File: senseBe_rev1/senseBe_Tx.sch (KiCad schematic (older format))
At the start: 18 parts, among them Q5 SI2302, Q6 SI2302, Q7 SI2302, U3 AP3403

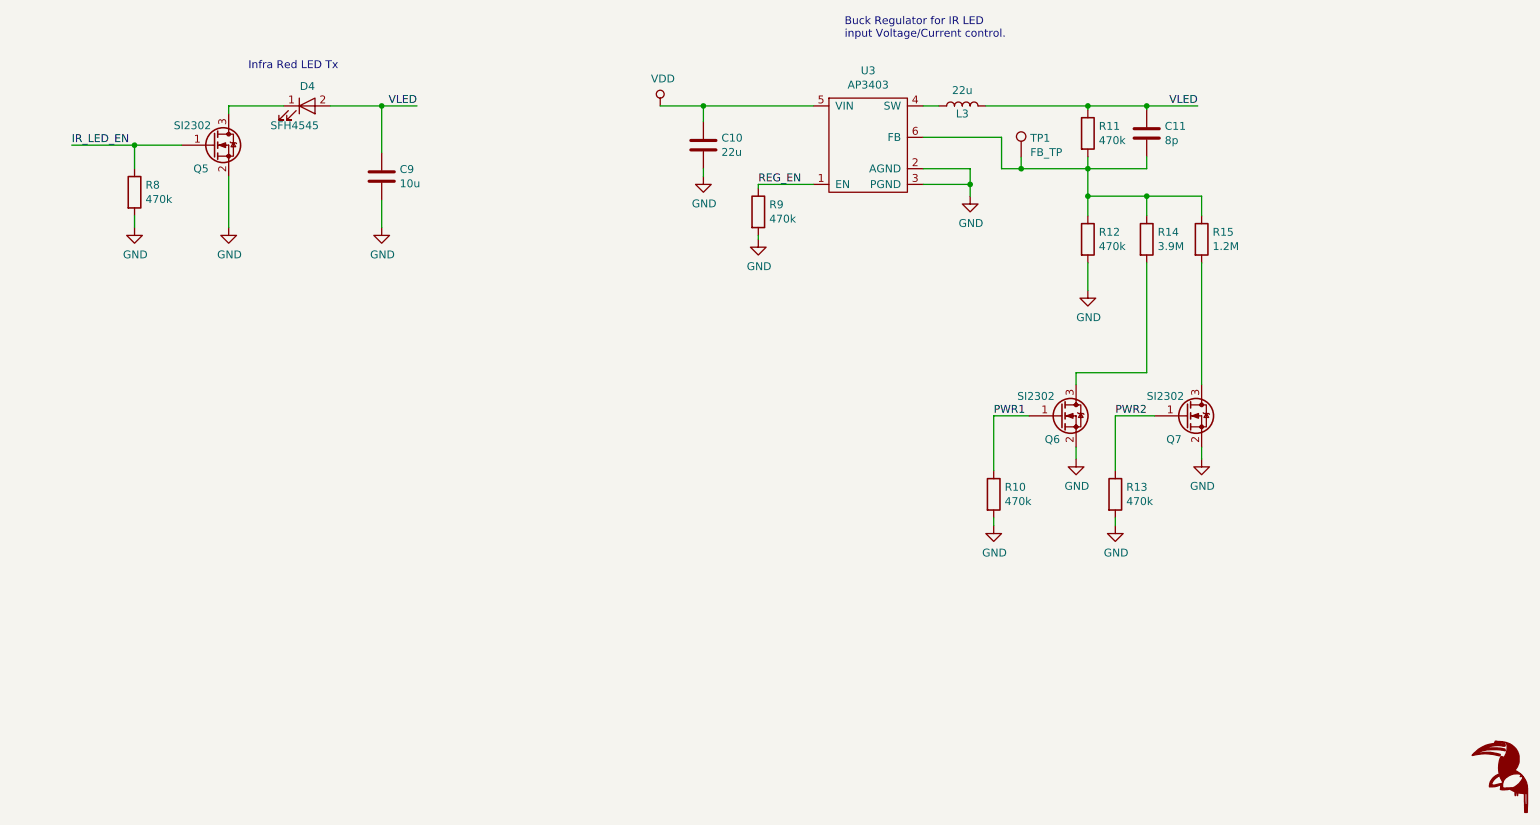
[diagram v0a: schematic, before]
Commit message: Completes Schematic and PCB Design.
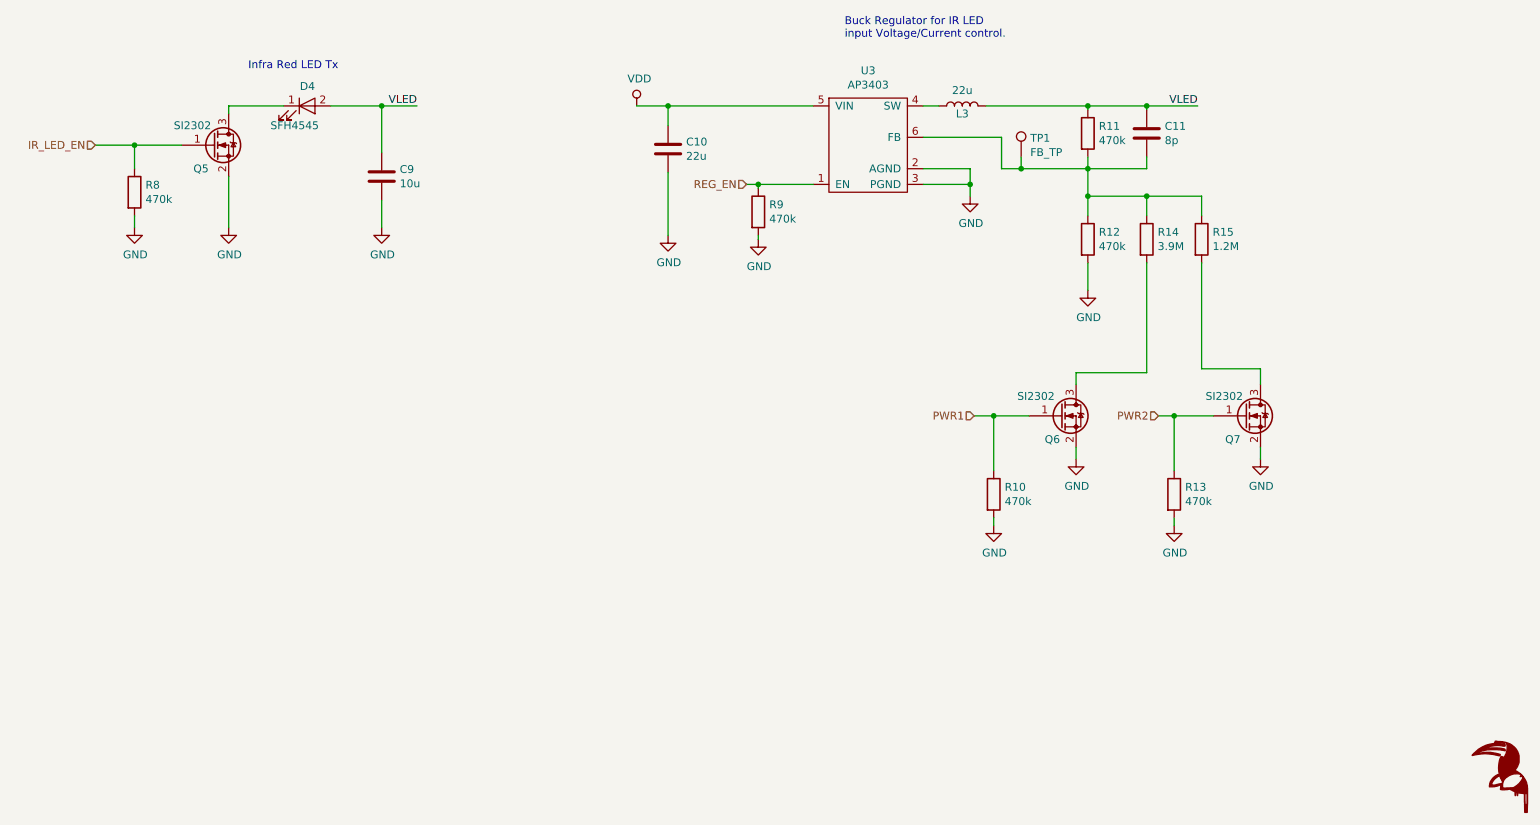
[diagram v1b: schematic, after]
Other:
- moved on the sheet: C10, Q7, R13
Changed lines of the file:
@@
 L senseBe_rev1-rescue:C-AP3403_LED_test-Ap3403_LED_test-rescue-senseBeTx_rev3-rescue-senseBe_rev1-rescue C?
 U 1 1 5C8021B2
-P 5775 2825
+P 5550 2850
 AR Path="/5C8021B2" Ref="C?"  Part="1"
 AR Path="/5C63BFE8/5C8021B2" Ref="C10"  Part="1"
-F 0 "C10" H 5890 2871 50  0000 L CNN
-F 1 "22u" H 5890 2780 50  0000 L CNN
-F 2 "senseBe_rev1_fp:C_0805_HandSoldering" H 5813 2675 50  0001 C CNN
-F 3 "~" H 5775 2825 50  0001 C CNN
-	1    5775 2825
+F 0 "C10" H 5665 2896 50  0000 L CNN
+F 1 "22u" H 5665 2805 50  0000 L CNN
+F 2 "senseBe_rev1_fp:C_0805_HandSoldering" H 5588 2700 50  0001 C CNN
+F 3 "~" H 5550 2850 50  0001 C CNN
+	1    5550 2850
 	1    0    0    -1
 $EndComp
@@
 L senseBe_rev1-rescue:GND-AP3403_LED_test-Ap3403_LED_test-rescue-senseBeTx_rev3-rescue-senseBe_rev1-rescue #PWR?
 U 1 1 5C8021CD
-P 5775 3025
+P 5550 3400
 AR Path="/5C8021CD" Ref="#PWR?"  Part="1"
 AR Path="/5C63BFE8/5C8021CD" Ref="#PWR0102"  Part="1"
-F 0 "#PWR0102" H 5775 2775 50  0001 C CNN
-F 1 "GND" H 5780 2852 50  0000 C CNN
-F 2 "" H 5775 3025 50  0001 C CNN
-F 3 "" H 5775 3025 50  0001 C CNN
-	1    5775 3025
-	1    0    0    -1
-$EndComp
-Wire Wire Line
-	5775 2975 5775 3025
-Wire Wire Line
-	5500 2575 5775 2575
-Wire Wire Line
-	5775 2575 5775 2675
-Text Label 6125 3075 0    50   ~ 0
-REG_EN
+F 0 "#PWR0102" H 5550 3150 50  0001 C CNN
+F 1 "GND" H 5555 3227 50  0000 C CNN
+F 2 "" H 5550 3400 50  0001 C CNN
+F 3 "" H 5550 3400 50  0001 C CNN
+	1    5550 3400
+	1    0    0    -1
+$EndComp
+Wire Wire Line
+	5550 3000 5550 3400
+Wire Wire Line
+	5350 2575 5550 2575
+Wire Wire Line
+	5550 2575 5550 2700
 Wire Wire Line
 	7175 2975 7475 2975
@@
 L senseBe_rev1-rescue:Q_NMOS_GSD-AP3403_LED_test-Ap3403_LED_test-rescue-senseBeTx_rev3-rescue-senseBe_rev1-rescue Q?
 U 1 1 5C80221D
-P 8850 4550
+P 9225 4550
 AR Path="/5C80221D" Ref="Q?"  Part="1"
 AR Path="/5C63BFE8/5C80221D" Ref="Q7"  Part="1"
-F 0 "Q7" H 8725 4400 50  0000 L CNN
-F 1 "SI2302" H 8600 4675 50  0000 L CNN
-F 2 "senseBeTx_rev3_fp:SOT-23_Handsoldering" H 9050 4650 50  0001 C CNN
-F 3 "~" H 8850 4550 50  0001 C CNN
-	1    8850 4550
+F 0 "Q7" H 9100 4400 50  0000 L CNN
+F 1 "SI2302" H 8975 4675 50  0000 L CNN
+F 2 "senseBeTx_rev3_fp:SOT-23_Handsoldering" H 9425 4650 50  0001 C CNN
+F 3 "~" H 9225 4550 50  0001 C CNN
+	1    9225 4550
 	1    0    0    -1
 $EndComp
@@
 L senseBe_rev1-rescue:GND-AP3403_LED_test-Ap3403_LED_test-rescue-senseBeTx_rev3-rescue-senseBe_rev1-rescue #PWR?
 U 1 1 5C80222B
-P 8950 4825
+P 9325 4825
 AR Path="/5C80222B" Ref="#PWR?"  Part="1"
 AR Path="/5C63BFE8/5C80222B" Ref="#PWR0106"  Part="1"
-F 0 "#PWR0106" H 8950 4575 50  0001 C CNN
-F 1 "GND" H 8955 4652 50  0000 C CNN
-F 2 "" H 8950 4825 50  0001 C CNN
-F 3 "" H 8950 4825 50  0001 C CNN
-	1    8950 4825
-	1    0    0    -1
-$EndComp
-Wire Wire Line
-	8950 4750 8950 4825
+F 0 "#PWR0106" H 9325 4575 50  0001 C CNN
+F 1 "GND" H 9330 4652 50  0000 C CNN
+F 2 "" H 9325 4825 50  0001 C CNN
+F 3 "" H 9325 4825 50  0001 C CNN
+	1    9325 4825
+	1    0    0    -1
+$EndComp
+Wire Wire Line
+	9325 4750 9325 4825
 Wire Wire Line
 	8150 4275 8150 4350
-Text Label 7625 4550 0    50   ~ 0
-PWR1
-Text Label 8400 4550 0    50   ~ 0
-PWR2
 $Comp
 L senseBe_rev1-rescue:Q_NMOS_GSD-AP3403_LED_test-Ap3403_LED_test-rescue-senseBeTx_rev3-rescue-senseBe_rev1-rescue Q?
@@
 Wire Wire Line
 	2750 3025 2750 3350
-Text Label 1750 2825 0    50   ~ 0
-IR_LED_EN
 Wire Wire Line
 	3725 3175 3725 3350
@@
 $EndComp
 Wire Wire Line
-	7625 4550 7625 4900
-Wire Wire Line
 	7625 5200 7625 5250
 $Comp
@@
 L senseBe_rev1-rescue:R-AP3403_LED_test-Ap3403_LED_test-rescue-senseBeTx_rev3-rescue-senseBe_rev1-rescue R?
 U 1 1 5C802266
-P 8400 5050
+P 8775 5050
 AR Path="/5C802266" Ref="R?"  Part="1"
 AR Path="/5C63BFE8/5C802266" Ref="R13"  Part="1"
-F 0 "R13" H 8470 5096 50  0000 L CNN
-F 1 "470k" H 8470 5005 50  0000 L CNN
-F 2 "senseBe_rev1_fp:R_0603_HandSoldering" V 8330 5050 50  0001 C CNN
-F 3 "~" H 8400 5050 50  0001 C CNN
-	1    8400 5050
-	1    0    0    -1
-$EndComp
-Wire Wire Line
-	8400 4900 8400 4550
-Wire Wire Line
-	8400 4550 8650 4550
+F 0 "R13" H 8845 5096 50  0000 L CNN
+F 1 "470k" H 8845 5005 50  0000 L CNN
+F 2 "senseBe_rev1_fp:R_0603_HandSoldering" V 8705 5050 50  0001 C CNN
+F 3 "~" H 8775 5050 50  0001 C CNN
+	1    8775 5050
+	1    0    0    -1
+$EndComp
+Wire Wire Line
+	8775 4900 8775 4550
+Wire Wire Line
+	8775 4550 9025 4550
 $Comp
 L senseBe_rev1-rescue:GND-AP3403_LED_test-Ap3403_LED_test-rescue-senseBeTx_rev3-rescue-senseBe_rev1-rescue #PWR?
 U 1 1 5C80226F
-P 8400 5250
+P 8775 5250
 AR Path="/5C80226F" Ref="#PWR?"  Part="1"
 AR Path="/5C63BFE8/5C80226F" Ref="#PWR0110"  Part="1"
-F 0 "#PWR0110" H 8400 5000 50  0001 C CNN
-F 1 "GND" H 8405 5077 50  0000 C CNN
-F 2 "" H 8400 5250 50  0001 C CNN
-F 3 "" H 8400 5250 50  0001 C CNN
-	1    8400 5250
+F 0 "#PWR0110" H 8775 5000 50  0001 C CNN
+F 1 "GND" H 8780 5077 50  0000 C CNN
+F 2 "" H 8775 5250 50  0001 C CNN
+F 3 "" H 8775 5250 50  0001 C CNN
+	1    8775 5250
 	1    0    0    -1
 $EndComp
@@
 L senseBe_rev1-rescue:VDD-senseBeRx_rev1-senseBeTx_rev3-rescue-senseBe_rev1-rescue #PWR?
 U 1 1 5C802290
-P 5500 2575
+P 5350 2575
 AR Path="/5C802290" Ref="#PWR?"  Part="1"
 AR Path="/5C63BFE8/5C802290" Ref="#PWR0112"  Part="1"
-F 0 "#PWR0112" H 5500 2425 50  0001 C CNN
-F 1 "VDD" H 5517 2748 50  0000 C CNN
-F 2 "" H 5500 2575 60  0000 C CNN
-F 3 "" H 5500 2575 60  0000 C CNN
-	1    5500 2575
+F 0 "#PWR0112" H 5350 2425 50  0001 C CNN
+F 1 "VDD" H 5367 2748 50  0000 C CNN
+F 2 "" H 5350 2575 60  0000 C CNN
+F 3 "" H 5350 2575 60  0000 C CNN
+	1    5350 2575
 	1    0    0    -1
 $EndComp
@@
 	2750 2575 3100 2575
 Wire Wire Line
-	8400 5200 8400 5250
+	8775 5200 8775 5250
 Wire Wire Line
 	7475 2975 7475 3075
@@
 	7475 3075 7475 3150
 Wire Wire Line
-	6475 2575 5775 2575
-Connection ~ 5775 2575
+	6475 2575 5550 2575
+Connection ~ 5550 2575
 Wire Wire Line
 	8225 2975 8225 3150
-Wire Wire Line
-	8950 3575 8950 4350
 Wire Wire Line
 	8600 3575 8600 4275
@@
 Connection ~ 3725 2575
 Wire Wire Line
-	1750 2825 2150 2825
+	1900 2825 2150 2825
 Connection ~ 2150 2825
 Wire Wire Line
@@
 	1    0    0    -1
 $EndComp
+Text HLabel 1900 2825 0    50   Input ~ 0
+IR_LED_EN
+Text HLabel 6050 3075 0    50   Input ~ 0
+REG_EN
+Wire Wire Line
+	6050 3075 6125 3075
+Connection ~ 6125 3075
+Text HLabel 7500 4550 0    50   Input ~ 0
+PWR1
+Text HLabel 8675 4550 0    50   Input ~ 0
+PWR2
+Wire Wire Line
+	7500 4550 7625 4550
+Connection ~ 7625 4550
+Wire Wire Line
+	8675 4550 8775 4550
+Wire Wire Line
+	7625 4550 7625 4900
+Connection ~ 8775 4550
+Wire Wire Line
+	8950 4250 9325 4250
+Wire Wire Line
+	8950 3575 8950 4250
+Wire Wire Line
+	9325 4250 9325 4350
 $EndSCHEMATC

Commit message: senseBe_rev2 PCB and Gerber files modified.
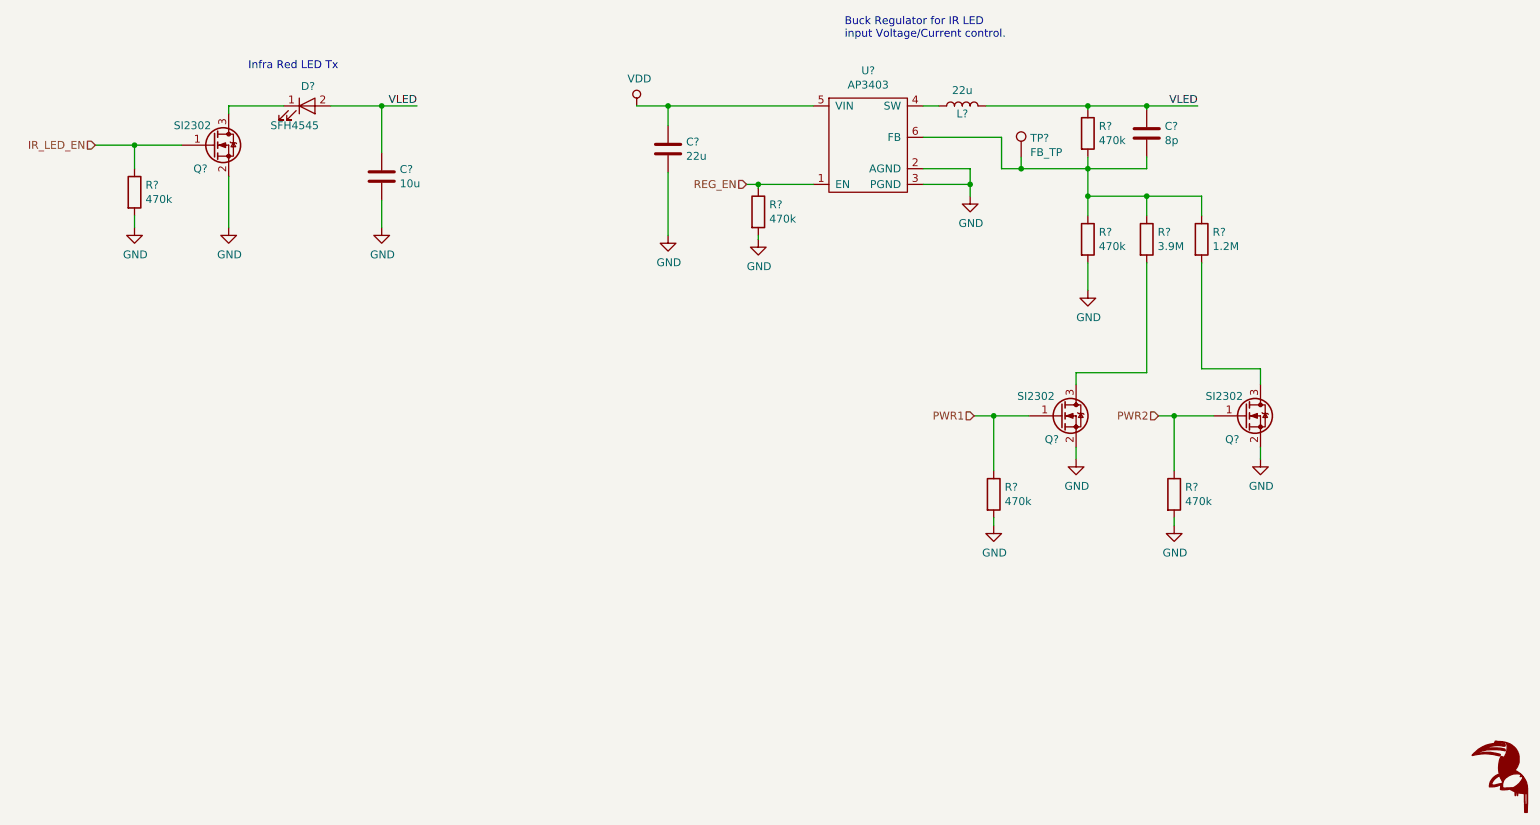
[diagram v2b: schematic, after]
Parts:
- renumbered C10 to C?, C11 to C?, C9 to C?, D4 to D?, L3 to L?, Q6 to Q?, Q7 to Q?, Q5 to Q?, R11 to R?, R12 to R?, R14 to R?, R15 to R?, R9 to R?, R10 to R?, R13 to R?, R8 to R?, TP1 to TP?, U3 to U?
